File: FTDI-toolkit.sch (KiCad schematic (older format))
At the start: 125 parts, among them IC1 TLV70033, IC13 74HC00BQ, IC15 TS5A3359, IC2 TLV70018, IC3 TS5A3359, J1 12401598E4_2A, J2 2X05, J3 2X08, J6 61300411121, Q1 NX3008CBKV, Q2 NX3008CBKV, SW1_A1 1X03, SW1_B1 1X03, SW2_A1 1X03, SW2_B1 1X03, U1 FT2232H-56Q, U10 74LVC2T45GT, U11 NTS0302JKZ, U2 SN74LVC1T45DRLR, U3 SN74LVC1T45DRLR, U4 TXB0104RUT, U5 74LVC2T45GT, U6 74LVC2T45GT, U7 74LVC2T45GT, U8 SN74LVC1T45DRLR, U9 SN74LVC1T45DRLR, Y1 ASFLMB-12.000MHZ-LC-T

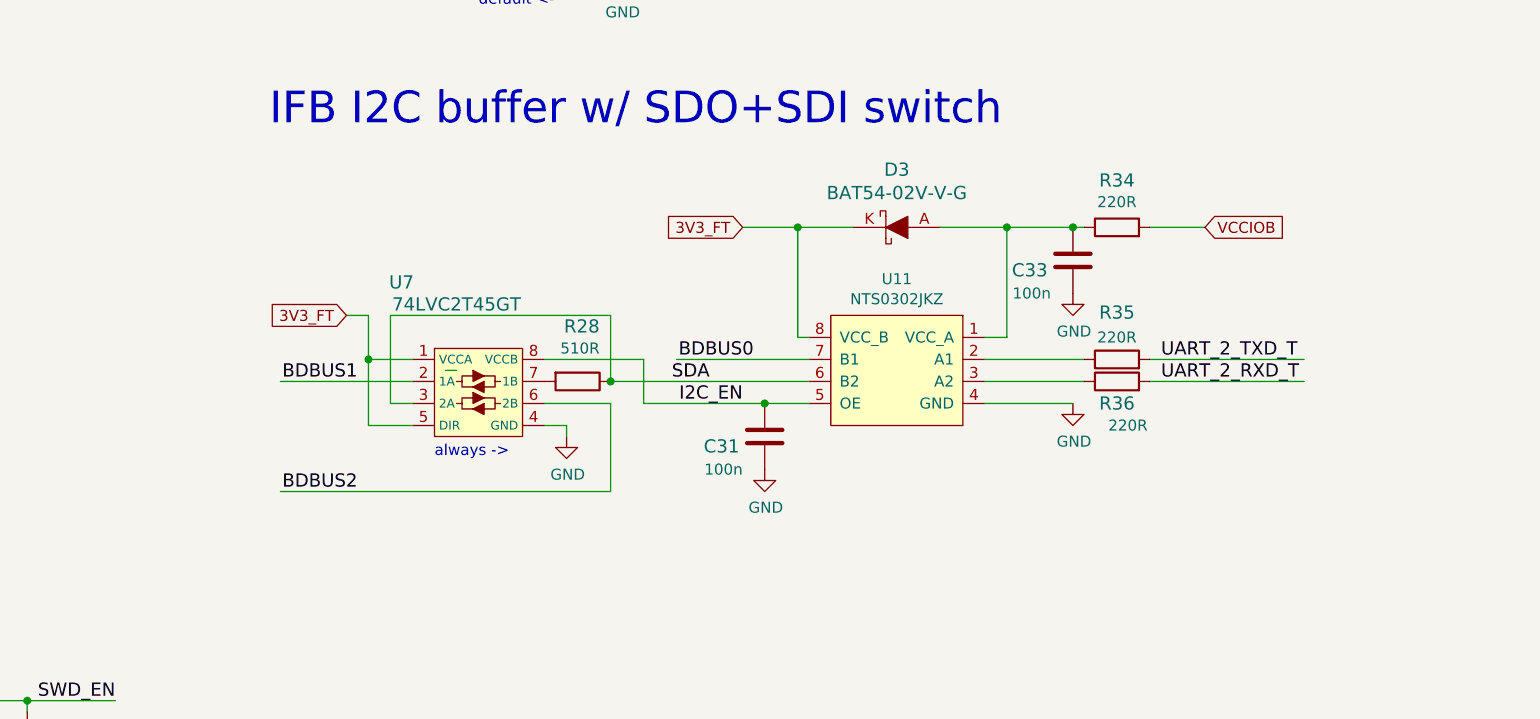
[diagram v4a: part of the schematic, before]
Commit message: R28 replaced with schottky diode. Changed C33 to 4u7 0402. Changes corrected on sch and pcb
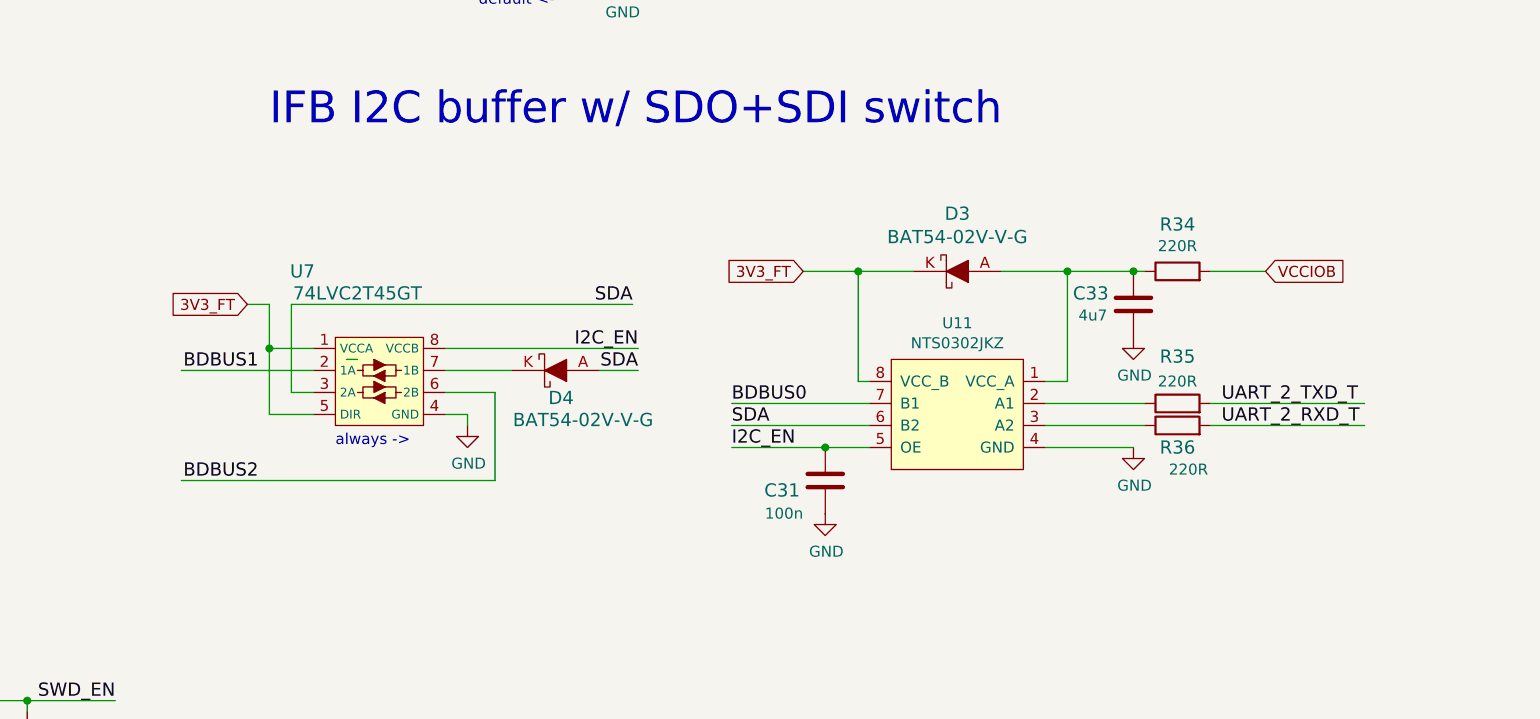
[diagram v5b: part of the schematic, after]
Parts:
- removed C33: C_100n_0402_16V, FTDI-toolkit-footprints:0402-cap, symbol FTDI-toolkit:C_100n_0402_16V
- removed R28: R_510_0402, FTDI-toolkit-footprints:0402-res, symbol FTDI-toolkit:R_510_0402
- added C33: C_4u7_0402, FTDI-toolkit-footprints:0402-cap, symbol FTDI-toolkit:C_4u7_0402
- added D4: BAT54-02V-V-G, FTDI-toolkit-footprints:SOD-523, symbol FTDI-toolkit:BAT54-02V-V-G
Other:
- moved on the sheet: C31, D3, R34, R35, R36, U11, U7

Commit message: Exchanged USB connector. Added switch and resistor for buffered SWD
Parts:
- removed J1: 12401598E4_2A, FTDI-toolkit-footprints:USB-C_Female_12401X, symbol FTDI-toolkit:12401598E4_2A
- added J1: USB4105-GF-A, antmicro-footprints:GCT_USB4105-GF-A, symbol antmicroUSBDVIHDMIConnectors:USB4105-GF-A
- added J4: M20-9990246, antmicro-footprints:PinHeader_1x2_P2.54mm, symbol antmicroRectangularConnectorsHeadersMalePins:M20-9990246
- added R28: R_510_0402, FTDI-toolkit-footprints:0402-res, symbol FTDI-toolkit:R_510_0402
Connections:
- wire segments 480 -> 466
- no-connect marks 19 -> 21
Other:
- note added: "SWD buffered mode switch"
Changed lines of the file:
@@
 	22500 5000 1000 5000
 Wire Wire Line
-	1400 2200 1400 3350
-Connection ~ 3300 2300
-Wire Wire Line
-	2800 2300 3300 2300
-Connection ~ 3200 2200
-Wire Wire Line
-	2800 2200 3200 2200
-$Comp
-L FTDI-toolkit:12401598E4_2A J1
-U 1 1 60256059
-P 2300 2250
-F 0 "J1" H 2300 3285 50  0000 C CNN
-F 1 "12401598E4_2A" H 2300 3194 50  0000 C CNN
-F 2 "FTDI-toolkit-footprints:USB-C_Female_12401X" H 2500 2450 60  0001 L CNN
-F 3 "http://www.amphenol-icc.com/media/wysiwyg/files/drawing/12401598xxx2a.pdf" H 2500 2550 60  0001 L CNN
-F 4 "12401598E4#2A" H 2500 2750 60  0001 L CNN "MPN"
-F 5 "Amphenol ICC (Commercial Products)" H 2500 3350 60  0001 L CNN "Manufacturer"
-	1    2300 2250
-	1    0    0    -1
-$EndComp
-Wire Wire Line
 	4300 2400 4300 2550
 Wire Wire Line
@@
 Wire Wire Line
 	3550 2000 3550 2350
-Connection ~ 3550 2000
 Wire Wire Line
 	3550 2000 3950 2000
 Wire Wire Line
-	4500 2300 5600 2300
-Wire Wire Line
-	4400 2200 5600 2200
-Wire Wire Line
-	3300 2300 4500 2300
-Wire Wire Line
-	3200 2200 4400 2200
-Connection ~ 4500 2300
+	4500 2325 5600 2325
 Wire Wire Line
-	4500 2550 4500 2300
+	4400 2175 5600 2175
 Wire Wire Line
-	3100 2000 3550 2000
+	4500 2550 4500 2325
 Wire Wire Line
 	2650 4150 2900 4150
@@
 	1    0    0    -1
 $EndComp
-Wire Wire Line
-	1600 2500 1600 3150
-Connection ~ 1600 2500
-Wire Wire Line
-	1800 2500 1600 2500
-Connection ~ 3100 2000
-Wire Wire Line
-	3100 3150 3100 2000
-Wire Wire Line
-	1600 3150 3100 3150
-Wire Wire Line
-	1600 2000 1600 2500
-Wire Wire Line
-	1800 2000 1600 2000
-Wire Wire Line
-	2900 2000 3100 2000
-Connection ~ 2900 2000
-Wire Wire Line
-	2900 2500 2900 2000
-Wire Wire Line
-	2800 2500 2900 2500
-Wire Wire Line
-	2800 2000 2900 2000
-Wire Wire Line
-	3300 3350 3300 2300
-Wire Wire Line
-	1400 3350 3300 3350
-Wire Wire Line
-	1800 2200 1400 2200
-Wire Wire Line
-	1500 2300 1800 2300
-Wire Wire Line
-	1500 3250 1500 2300
-Wire Wire Line
-	3200 3250 1500 3250
-Wire Wire Line
-	3200 2200 3200 3250
-Wire Wire Line
-	2100 3200 2100 3450
-$Comp
-L FTDI-toolkit:GNDREF #PWR0139
-U 1 1 5F66E573
-P 2100 3450
-F 0 "#PWR0139" H 2100 3200 50  0001 C CNN
-F 1 "GNDREF" H 2105 3277 50  0000 C CNN
-F 2 "" H 2100 3450 50  0001 C CNN
-F 3 "" H 2100 3450 50  0001 C CNN
-	1    2100 3450
-	1    0    0    -1
-$EndComp
-Connection ~ 3000 2800
-Wire Wire Line
-	3000 1700 3000 2800
-Wire Wire Line
-	2800 1700 3000 1700
-Connection ~ 1700 2800
-Wire Wire Line
-	1700 1700 1700 2800
-Wire Wire Line
-	1800 1700 1700 1700
-Wire Wire Line
-	3000 2800 3000 2900
-Wire Wire Line
-	2800 2800 3000 2800
-Wire Wire Line
-	1700 2800 1700 2900
-Wire Wire Line
-	1800 2800 1700 2800
-$Comp
-L FTDI-toolkit:GND #PWR0134
-U 1 1 5F5AAFDD
-P 1700 2900
-F 0 "#PWR0134" H 1700 2650 50  0001 C CNN
-F 1 "GND" H 1705 2727 50  0000 C CNN
-F 2 "" H 1700 2900 50  0001 C CNN
-F 3 "" H 1700 2900 50  0001 C CNN
-	1    1700 2900
-	1    0    0    -1
-$EndComp
-$Comp
-L FTDI-toolkit:GND #PWR0126
-U 1 1 5F5A9AB0
-P 3000 2900
-F 0 "#PWR0126" H 3000 2650 50  0001 C CNN
-F 1 "GND" H 3005 2727 50  0000 C CNN
-F 2 "" H 3000 2900 50  0001 C CNN
-F 3 "" H 3000 2900 50  0001 C CNN
-	1    3000 2900
-	1    0    0    -1
-$EndComp
 $Comp
 L FTDI-toolkit:LG_L29K-G2J1-24-Z USB1
@@
 U 1 1 5E5F7C2B
 P 4150 2000
-F 0 "L1" H 4000 2050 60  0000 R BNN
-F 1 "BLM18PG121SN1D" H 4050 2100 60  0000 L BNN
+F 0 "L1" H 4300 2125 60  0000 R BNN
+F 1 "BLM18PG121SN1D" H 3325 2125 60  0000 L BNN
 F 2 "FTDI-toolkit-footprints:0603-res" H 4050 2100 60  0001 C CNN
 F 3 "https://www.murata.com/en-us/products/productdata/8796738650142/ENFA0003.pdf" H 4050 2100 60  0001 C CNN
@@
 Wire Wire Line
 	4950 2400 4950 2000
-Connection ~ 4400 2200
+Connection ~ 4400 2175
 Wire Wire Line
-	4400 2550 4400 2200
+	4400 2550 4400 2175
 Wire Wire Line
 	4350 2000 4950 2000
@@
 Text GLabel 5950 1650 1    50   Input ~ 0
 5V_USB
-Text Label 5050 2200 0    60   ~ 0
+Text Label 5600 2175 2    60   ~ 0
 USB_D_P
-Text Label 5050 2300 0    60   ~ 0
+Text Label 5600 2325 2    60   ~ 0
 USB_D_N
 Text Notes 7550 2950 0    144  ~ 0
@@
 Wire Wire Line
 	14200 12950 13900 12950
+$Comp
+L antmicroUSBDVIHDMIConnectors:USB4105-GF-A J1
+U 1 1 62BA78DC
+P 2150 2575
+F 0 "J1" H 2557 3842 50  0000 C CNN
+F 1 "USB4105-GF-A" H 2557 3751 50  0000 C CNN
+F 2 "antmicro-footprints:GCT_USB4105-GF-A" H 1500 2825 50  0001 L BNN
+F 3 "https://gct.co/files/drawings/usb4105.pdf" H 2150 2575 50  0001 L BNN
+F 4 "GCT" H 1500 2925 50  0001 L BNN "Manufacturer"
+F 5 "USB4105-GF-A" H 1800 3025 50  0001 C CNN "MPN"
+	1    2150 2575
+	1    0    0    -1
+$EndComp
+NoConn ~ 2950 2575
+NoConn ~ 2950 2675
+$Comp
+L FTDI-toolkit:GNDREF #PWR0105
+U 1 1 62C41BFB
+P 3000 3050
+F 0 "#PWR0105" H 3000 2800 50  0001 C CNN
+F 1 "GNDREF" H 3005 2877 50  0000 C CNN
+F 2 "" H 3000 3050 50  0001 C CNN
+F 3 "" H 3000 3050 50  0001 C CNN
+	1    3000 3050
+	1    0    0    -1
+$EndComp
+Wire Wire Line
+	3000 3050 3000 2975
+Wire Wire Line
+	3000 2975 2950 2975
+$Comp
+L FTDI-toolkit:GND #PWR0109
+U 1 1 62C8C6B7
+P 3275 3050
+F 0 "#PWR0109" H 3275 2800 50  0001 C CNN
+F 1 "GND" H 3280 2877 50  0000 C CNN
+F 2 "" H 3275 3050 50  0001 C CNN
+F 3 "" H 3275 3050 50  0001 C CNN
+	1    3275 3050
+	1    0    0    -1
+$EndComp
+Wire Wire Line
+	3275 3050 3275 2875
+Wire Wire Line
+	3275 2875 2950 2875
+Wire Wire Line
+	2950 2425 3050 2425
+Wire Wire Line
+	3050 2425 3050 2325
+Wire Wire Line
+	3050 2325 2950 2325
+Wire Wire Line
+	2950 2075 3050 2075
+Wire Wire Line
+	3050 2075 3050 2175
+Wire Wire Line
+	3050 2175 2950 2175
+Connection ~ 4500 2325
+Wire Wire Line
+	3050 2175 4400 2175
+Connection ~ 3050 2175
+Wire Wire Line
+	3050 2325 4500 2325
+Connection ~ 3050 2325
+Wire Wire Line
+	3550 2000 3375 2000
+Wire Wire Line
+	3375 2000 3375 1625
+Wire Wire Line
+	3375 1625 2950 1625
+Connection ~ 3550 2000
+Text Label 14025 14825 0    60   ~ 0
+UART_1_RXD_T
+Text Label 14025 14925 0    60   ~ 0
+UART_1_RTS_T
+$Comp
+L FTDI-toolkit:R_510_0402 R28
+U 1 1 6336BFB1
+P 14875 14825
+F 0 "R28" H 14875 15038 60  0000 C CNN
+F 1 "R_510_0402" H 14875 14675 60  0001 C CNN
+F 2 "FTDI-toolkit-footprints:0402-res" H 15075 15025 60  0001 L CNN
+F 3 "" H 14875 14825 50  0001 C CNN
+F 4 "Vishay" H 15075 15225 60  0001 L CNN "Manufacturer"
+F 5 "CRCW0402510RFKEDC" H 15075 15125 60  0001 L CNN "MPN"
+F 6 "510" H 14875 14940 50  0000 C CNN "Val"
+	1    14875 14825
+	1    0    0    -1
+$EndComp
+Wire Wire Line
+	14025 14825 14725 14825
+Wire Wire Line
+	15025 14825 15150 14825
+Wire Wire Line
+	14025 14925 15150 14925
+Text Notes 13475 14450 0    144  ~ 0
+SWD buffered mode switch
+$Comp
+L antmicroRectangularConnectorsHeadersMalePins:M20-9990246 J4
+U 1 1 6352EADF
+P 15250 14925
+F 0 "J4" V 15341 14797 50  0000 R CNN
+F 1 "M20-9990246" V 15250 14797 50  0000 R CNN
+F 2 "antmicro-footprints:PinHeader_1x2_P2.54mm" H 15450 15125 60  0001 L CNN
+F 3 "https://cdn.harwin.com/pdfs/M20-999.pdf" H 15450 15225 60  0001 L CNN
+F 4 "M20-9990246" H 15450 15425 60  0001 L CNN "MPN"
+F 5 "Harwin Inc." H 15450 16025 60  0001 L CNN "Manufacturer"
+	1    15250 14925
+	0    -1   -1   0
+$EndComp
 $EndSCHEMATC

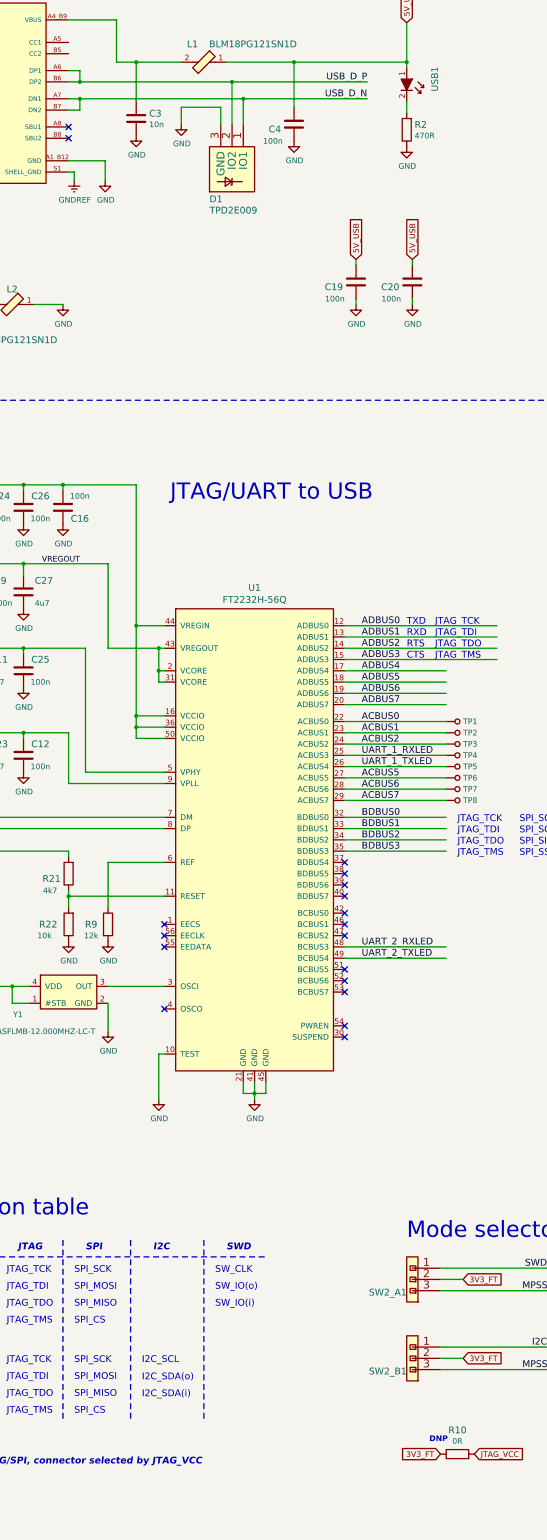
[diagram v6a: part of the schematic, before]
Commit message: Layout review: fixed DNP, minot layout/placement issues, marking
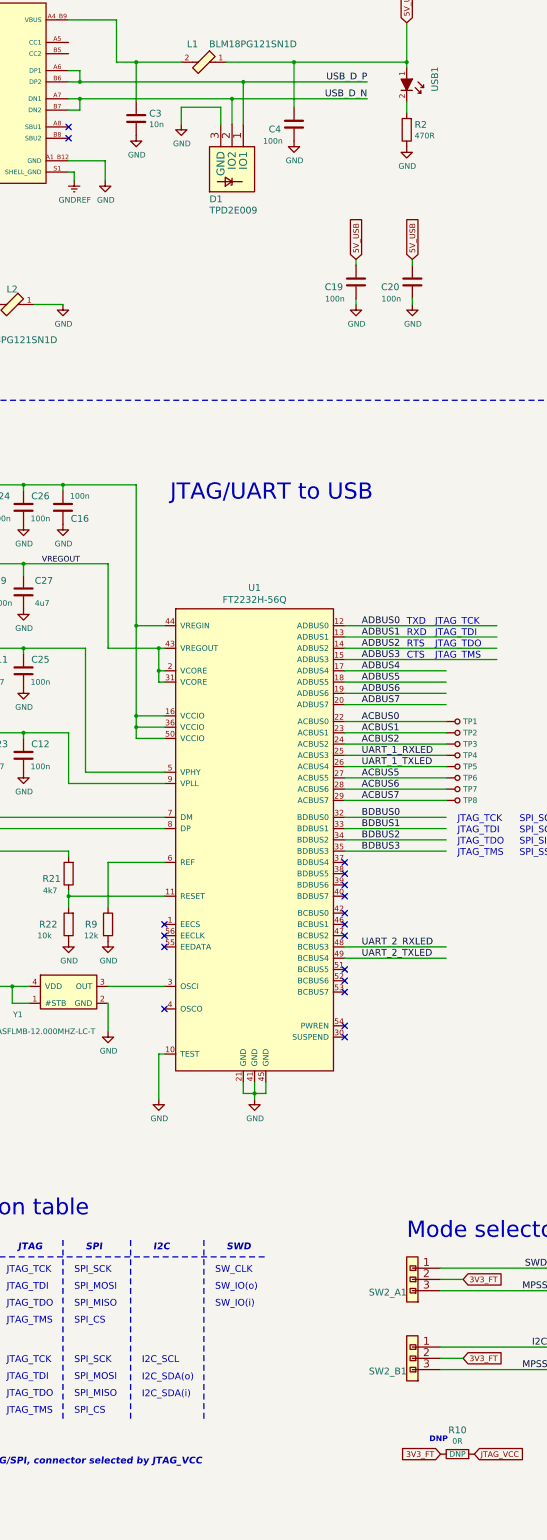
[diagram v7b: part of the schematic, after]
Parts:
- R10: DNP 1 -> DNP
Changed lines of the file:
@@
 	3550 2000 3950 2000
 Wire Wire Line
-	4500 2325 5600 2325
-Wire Wire Line
-	4400 2175 5600 2175
-Wire Wire Line
-	4500 2550 4500 2325
-Wire Wire Line
 	2650 4150 2900 4150
 Wire Wire Line
@@
 $EndComp
 $Comp
-L FTDI-toolkit:TPD2E009 D1
-U 1 1 5E5F7BFF
-P 4500 2750
-F 0 "D1" V 5000 2450 60  0000 L BNN
-F 1 "TPD2E009" V 5100 2450 60  0000 L BNN
-F 2 "FTDI-toolkit-footprints:SOT-3" H 5100 2450 60  0001 C CNN
-F 3 "https://www.ti.com/lit/ds/symlink/tpd2e009.pdf?ts=1597910439511&ref_url=https%253A%252F%252Fwww.google.com%252F" H 5100 2450 60  0001 C CNN
-F 4 "TPD2E009DRTR" H 1700 500 50  0001 C CNN "MPN"
-F 5 "Texas Instruments" H 1700 500 50  0001 C CNN "Manufacturer"
-	1    4500 2750
-	0    1    1    0
-$EndComp
-$Comp
 L FTDI-toolkit:R_470R_0402 R2
 U 1 1 5E960659
@@
 Wire Wire Line
 	4950 2400 4950 2000
-Connection ~ 4400 2175
-Wire Wire Line
-	4400 2550 4400 2175
 Wire Wire Line
 	4350 2000 4950 2000
@@
 F 5 "CR0603-J/-000ELF" H 6600 14650 60  0001 L CNN "MPN"
 F 6 "0R" H 6400 14465 50  0000 C CNN "Val"
-F 7 "1" H 6400 14350 50  0001 C CNN "DNP"
+F 7 "DNP" H 6400 14350 50  0000 C CNN "DNP"
 	1    6400 14350
 	1    0    0    -1
@@
 Wire Wire Line
 	3050 2175 2950 2175
-Connection ~ 4500 2325
-Wire Wire Line
-	3050 2175 4400 2175
 Connection ~ 3050 2175
-Wire Wire Line
-	3050 2325 4500 2325
 Connection ~ 3050 2325
 Wire Wire Line
@@
 	0    -1   -1   0
 $EndComp
+Wire Wire Line
+	3050 2325 4400 2325
+Wire Wire Line
+	3050 2175 4500 2175
+$Comp
+L FTDI-toolkit:TPD2E009 D1
+U 1 1 5E5F7BFF
+P 4500 2750
+F 0 "D1" V 5000 2450 60  0000 L BNN
+F 1 "TPD2E009" V 5100 2450 60  0000 L BNN
+F 2 "FTDI-toolkit-footprints:SOT-3" H 5100 2450 60  0001 C CNN
+F 3 "https://www.ti.com/lit/ds/symlink/tpd2e009.pdf?ts=1597910439511&ref_url=https%253A%252F%252Fwww.google.com%252F" H 5100 2450 60  0001 C CNN
+F 4 "TPD2E009DRTR" H 1700 500 50  0001 C CNN "MPN"
+F 5 "Texas Instruments" H 1700 500 50  0001 C CNN "Manufacturer"
+	1    4500 2750
+	0    1    1    0
+$EndComp
+Wire Wire Line
+	4400 2550 4400 2325
+Connection ~ 4400 2325
+Wire Wire Line
+	4400 2325 5600 2325
+Wire Wire Line
+	4500 2550 4500 2175
+Connection ~ 4500 2175
+Wire Wire Line
+	4500 2175 5600 2175
 $EndSCHEMATC
